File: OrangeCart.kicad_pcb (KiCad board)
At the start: 6 copper layers, 62 x 50 mm, 131 parts, among them J1 Conn_02x11_Odd_Even, J2 UART, J3 USB_B_Mini, J4 MicroSd, J6 JTAG, SW1 SW_Push, U1 FAN53541, U10 NCP115-2.5, U11 74AHCV17A, U12 74LVC3G17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

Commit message: Connect some unconnected stuff
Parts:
- moved R4 5.64 mm to (64.3, 95.2), turned to 270 degrees
- moved C24 5.44 mm to (63.4, 88.7), turned to 90 degrees
- moved FB3 4.57 mm to (63.4, 93.6), turned to 270 degrees
- moved C31 1.69 mm to (63.7, 91.0), turned to 180 degrees
- moved C22 0.58 mm to (63.4, 91.7), turned to 270 degrees
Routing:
- net /sheetHyperRAM/RAM_VCC: track 6.70 -> 27.9 mm
- net /sheetHyperRAM/RAM_VCCQ: track 11.7 -> 18.5 mm
- net P1.8V: track 80.8 -> 85.3 mm, vias 12 -> 11
- net GND: track 141.6 -> 145.1 mm, vias 112 -> 115
- net USER_BUTTON: track 21.3 -> 22.9 mm
- added copper zone on In3.Cu, net /sheetHyperRAM/RAM_VCC
- added copper zone on In3.Cu, net /sheetHyperRAM/RAM_VCCQ

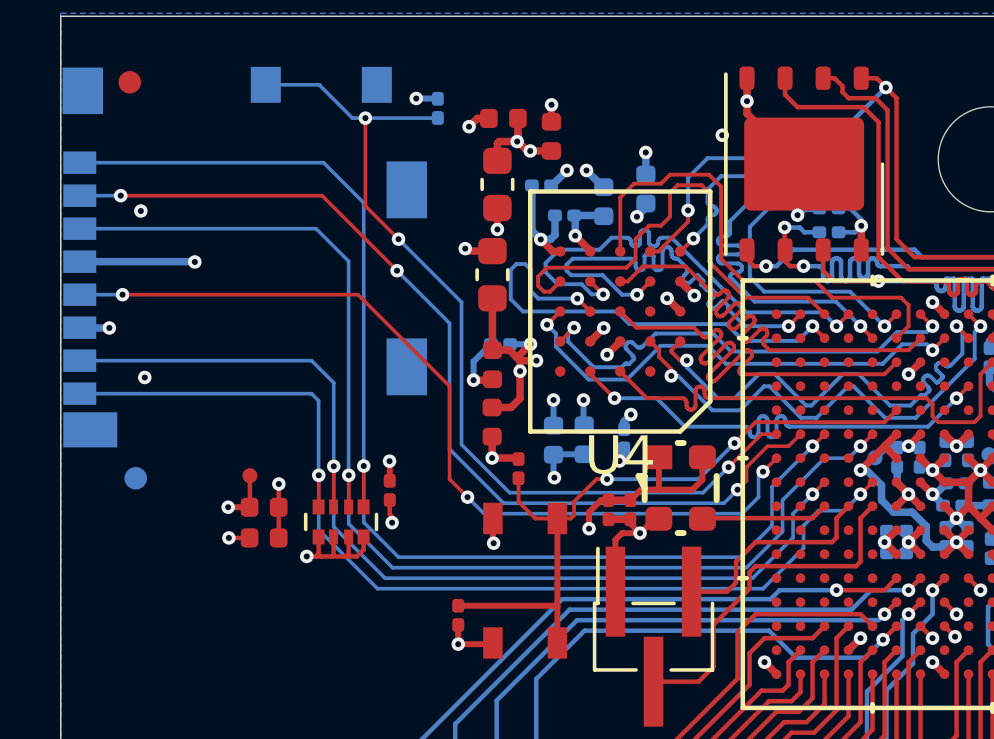
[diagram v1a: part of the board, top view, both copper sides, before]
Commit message: Length match SDCARD
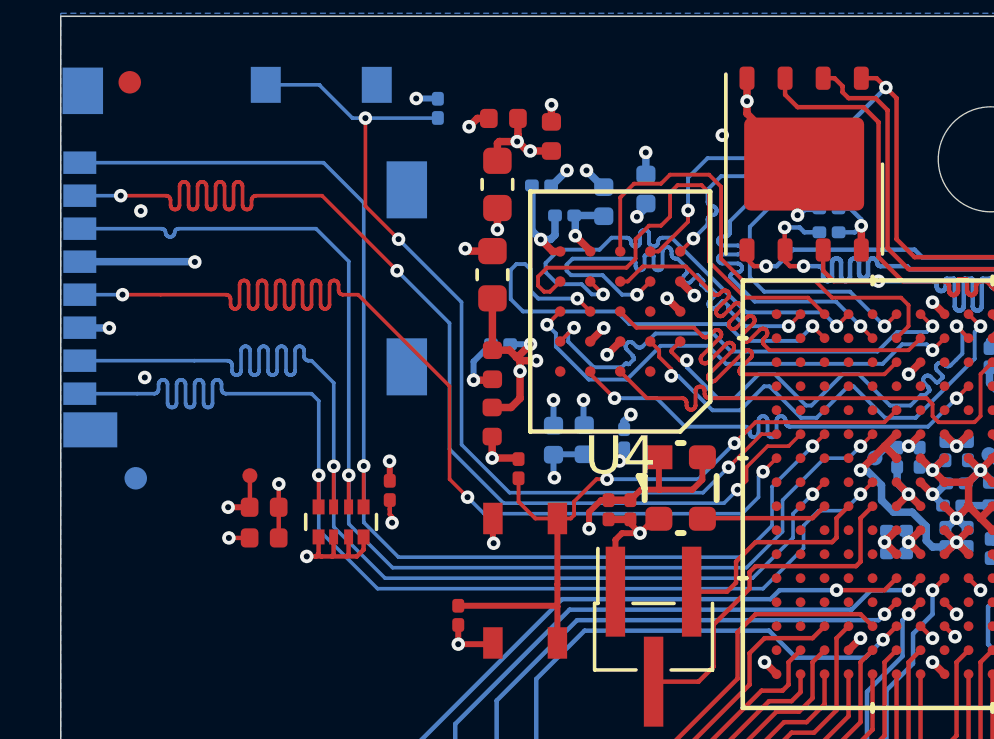
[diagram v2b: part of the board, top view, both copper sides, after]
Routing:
- net SD0_CLK: track 29.2 -> 39.0 mm
- net SD0_DAT3: track 31.9 -> 39.0 mm
- net SD0_DAT0: track 33.8 -> 40.3 mm
- net SD0_DAT1: track 34.6 -> 40.0 mm

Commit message: Reduce layers to 4
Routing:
- added copper zone on In2.Cu, net /sheetHyperRAM/RAM_VCC
- added copper zone on In2.Cu, net /sheetHyperRAM/RAM_VCCQ
- added copper zone on In2.Cu, net Net-(C29-Pad2)
- added copper zone on In2.Cu, net P5.0V
- added copper zone on In2.Cu, net PUSB_VBUS
- removed copper zone on In3.Cu, net /sheetHyperRAM/RAM_VCC
- removed copper zone on In3.Cu, net /sheetHyperRAM/RAM_VCCQ
- removed copper zone on In3.Cu, net GND
- removed copper zone on In4.Cu, net GND
- removed copper zone on In3.Cu, net Net-(C29-Pad2)
- removed copper zone on In3.Cu, net P1.1V
- removed copper zone on In4.Cu, net P1.1V
- removed copper zone on In3.Cu, net P1.8V
- removed copper zone on In4.Cu, net P1.8V
- removed copper zone on In3.Cu, net P3.3V
- removed copper zone on In4.Cu, net P3.3V
- removed copper zone on In3.Cu, net P5.0V
- removed copper zone on In3.Cu, net PUSB_VBUS
- removed copper zone on In3.Cu, net VSYS
- removed copper zone on In4.Cu, net VSYS
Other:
- copper layers 6 -> 4
- rule via_min_drill: 0.15 -> 0.2

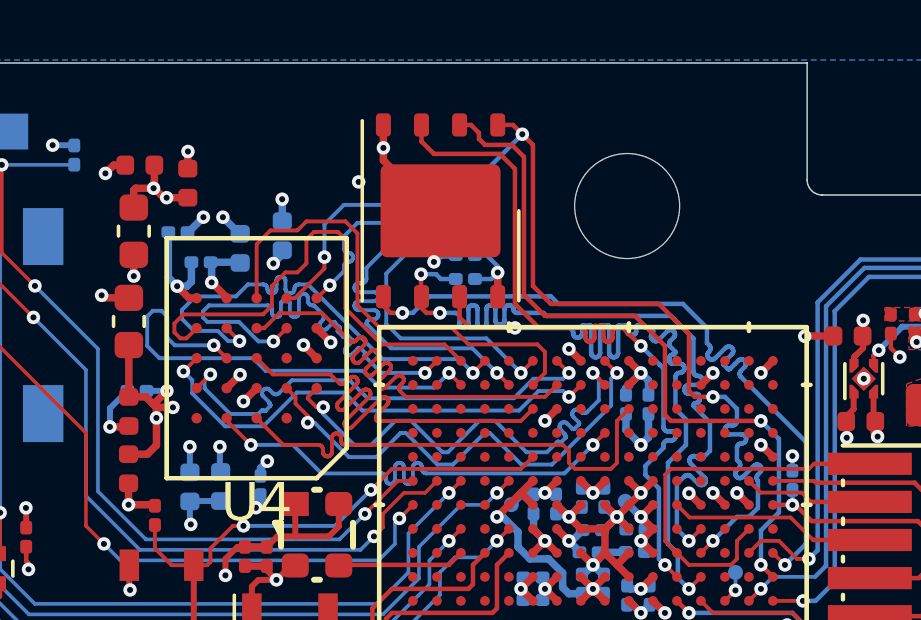
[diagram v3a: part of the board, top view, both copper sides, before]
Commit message: Hook up last two GND pins
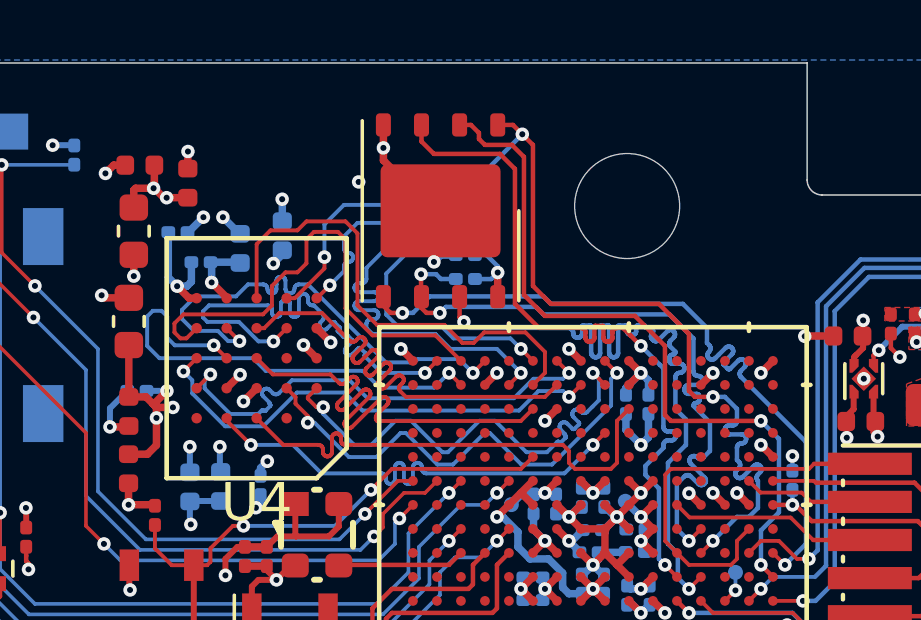
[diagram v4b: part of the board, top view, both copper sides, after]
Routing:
- net SPI_CONFIG_SCK: track 26.7 -> 23.4 mm
- net GND: track 145.1 -> 146.2 mm, vias 115 -> 117
- net RAM_DQ7: track 16.2 -> 17.0 mm
- net RAM_DQ6: track 16.1 -> 15.6 mm

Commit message: Retune track lengths
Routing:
- net SPI_CONFIG_SCK: track 23.4 -> 26.7 mm
- net RAM_DQ7: track 17.0 -> 16.2 mm
- net RAM_DQ6: track 15.6 -> 16.2 mm

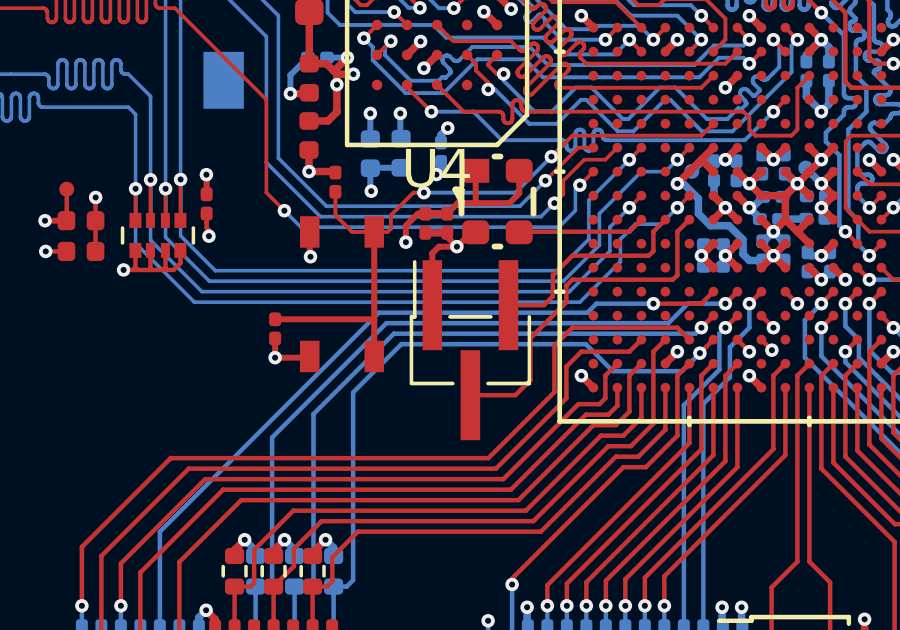
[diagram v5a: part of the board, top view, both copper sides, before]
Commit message: Rotate UART connector
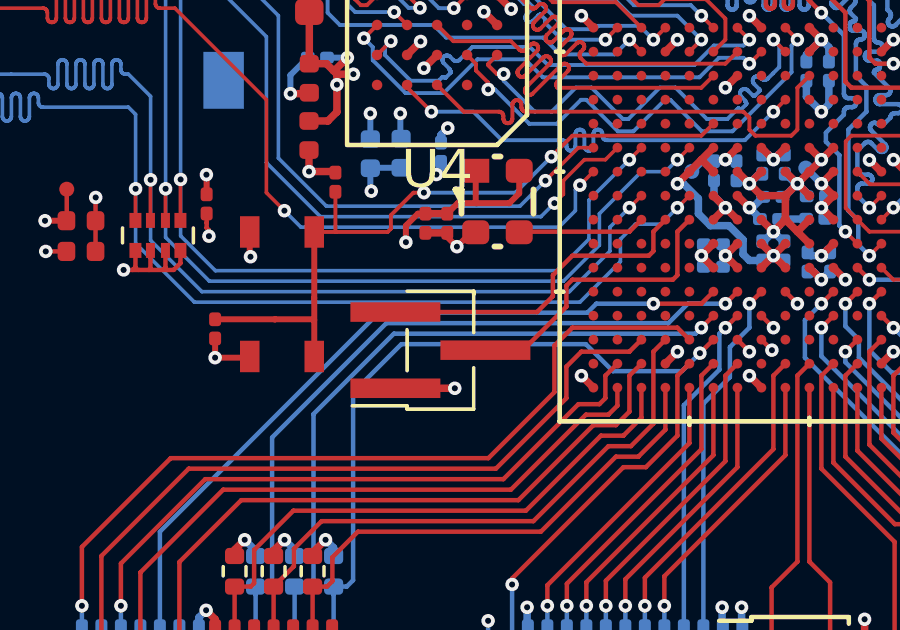
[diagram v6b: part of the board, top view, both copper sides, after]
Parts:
- moved SW1 2.00 mm to (62.5, 98.9)
- moved C76 2.00 mm to (60.2, 100.1)
- moved J2 1.00 mm to (67.8, 100.8), turned to 180 degrees
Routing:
- net /sheetFPGA/TXD: track 7.20 -> 11.1 mm
- net /sheetFPGA/RXD: track 11.7 -> 9.86 mm
- net USER_BUTTON: track 22.9 -> 23.9 mm
- net GND: track 146.2 -> 145.5 mm, vias 117 -> 118
